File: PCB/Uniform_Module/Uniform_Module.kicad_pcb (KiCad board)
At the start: 2 copper layers, 33 x 16 mm, 17 parts, among them J1 PCIE_x1_Conn_01x36_Male, SW1 Button_SMD_PTS_647_SN50_SMTR2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, SW2 Button_SMD_PTS_647_SN50_SMTR2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, U1 STM32L072KZT6

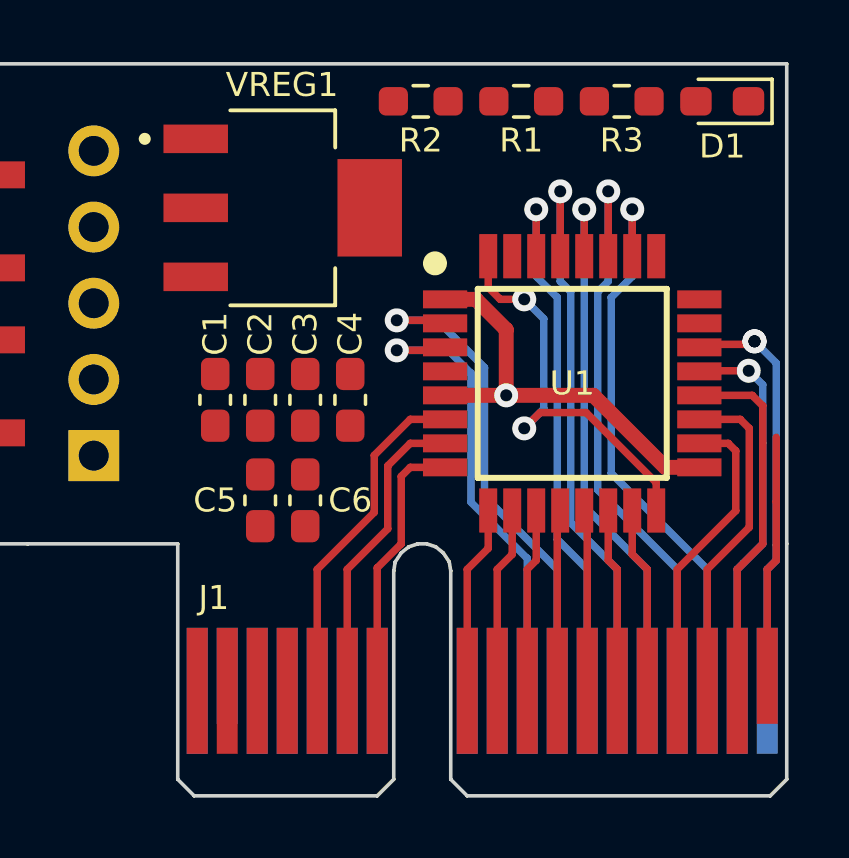
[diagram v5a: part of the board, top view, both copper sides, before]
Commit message: uniform module routing half done
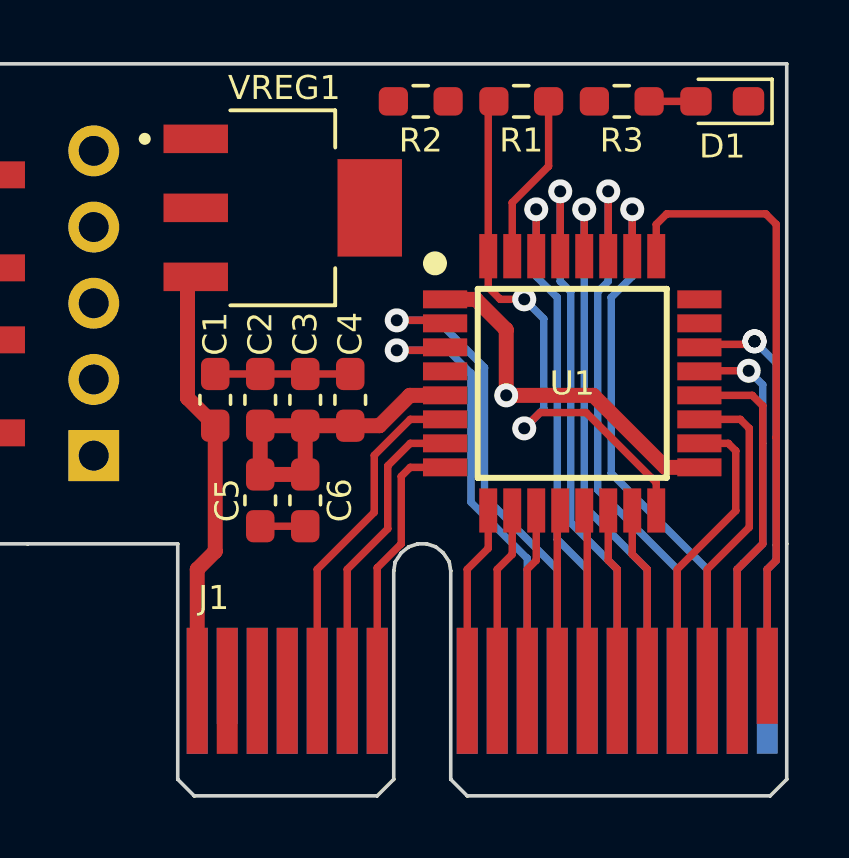
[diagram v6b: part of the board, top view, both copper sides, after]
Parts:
- turned C2 to 90 degrees
- turned C3 to 90 degrees
- turned C4 to 90 degrees
- turned C5 to -90 degrees
- turned C6 to -90 degrees
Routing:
- net +5V: track 0.00 -> 14.6 mm
- net PA15: track 8.07 -> 20.5 mm
- net GND: track 13.8 -> 25.1 mm
- net +3V3: track 14.1 -> 23.5 mm
- net BOOT: track 0.00 -> 5.66 mm
- net Net-(D1-Pad2): track 0.00 -> 1.56 mm

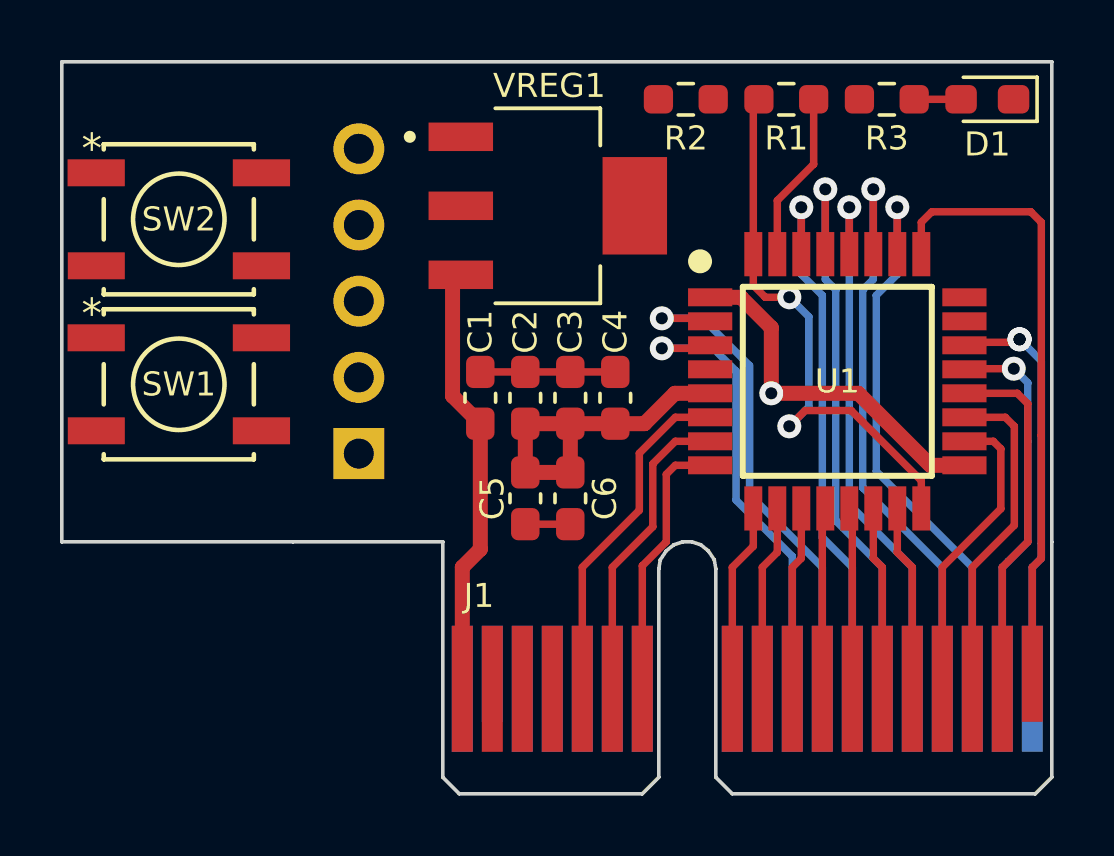
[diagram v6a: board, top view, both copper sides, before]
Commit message: Uniform module traces first pass complete
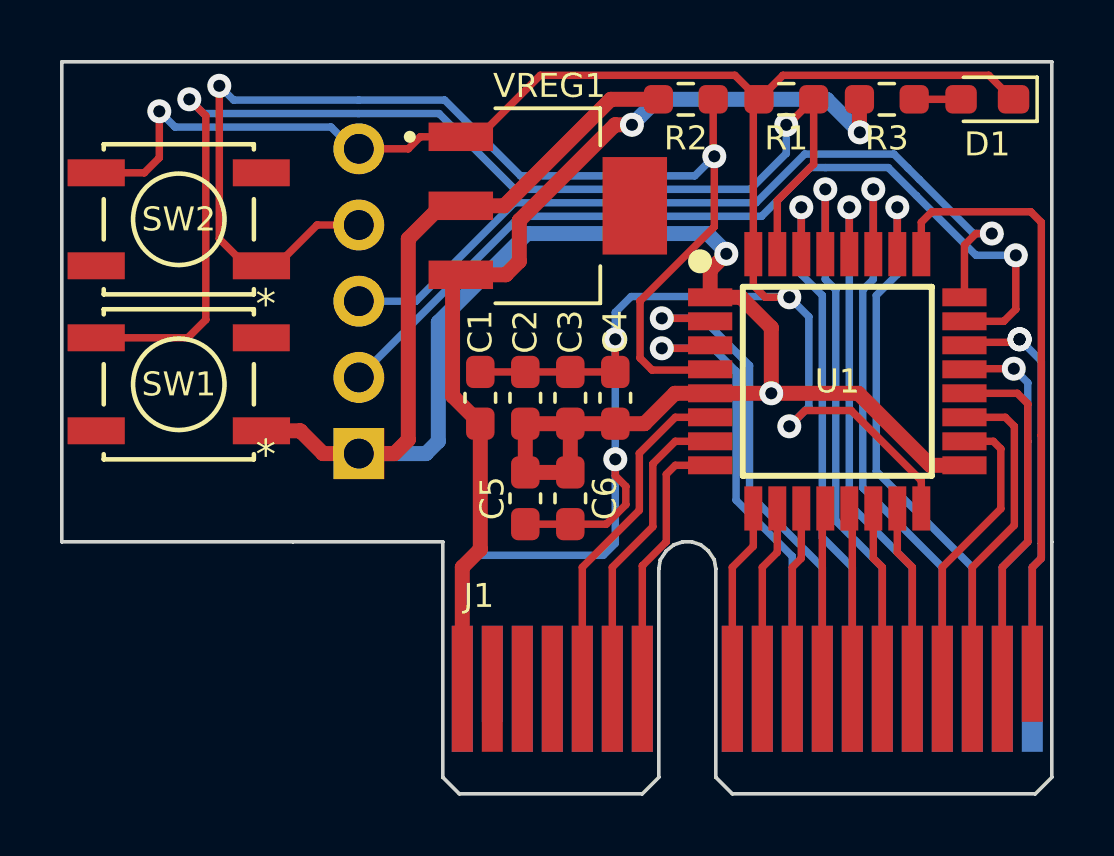
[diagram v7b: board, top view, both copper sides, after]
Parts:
- turned SW1 to 180 degrees
- turned SW2 to 180 degrees
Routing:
- net GND: track 25.1 -> 88.0 mm, vias 2 -> 5
- net +3V3: track 23.5 -> 67.5 mm, vias 1 -> 2
- net RESET: track 0.00 -> 40.9 mm, vias 0 -> 2
- net BOOT: track 5.66 -> 41.0 mm, vias 0 -> 2
- net SWDIO: track 0.00 -> 29.7 mm, vias 0 -> 1
- net SWCLK: track 0.00 -> 27.0 mm, vias 0 -> 1
- net +5V: track 14.6 -> 32.7 mm, vias 0 -> 2

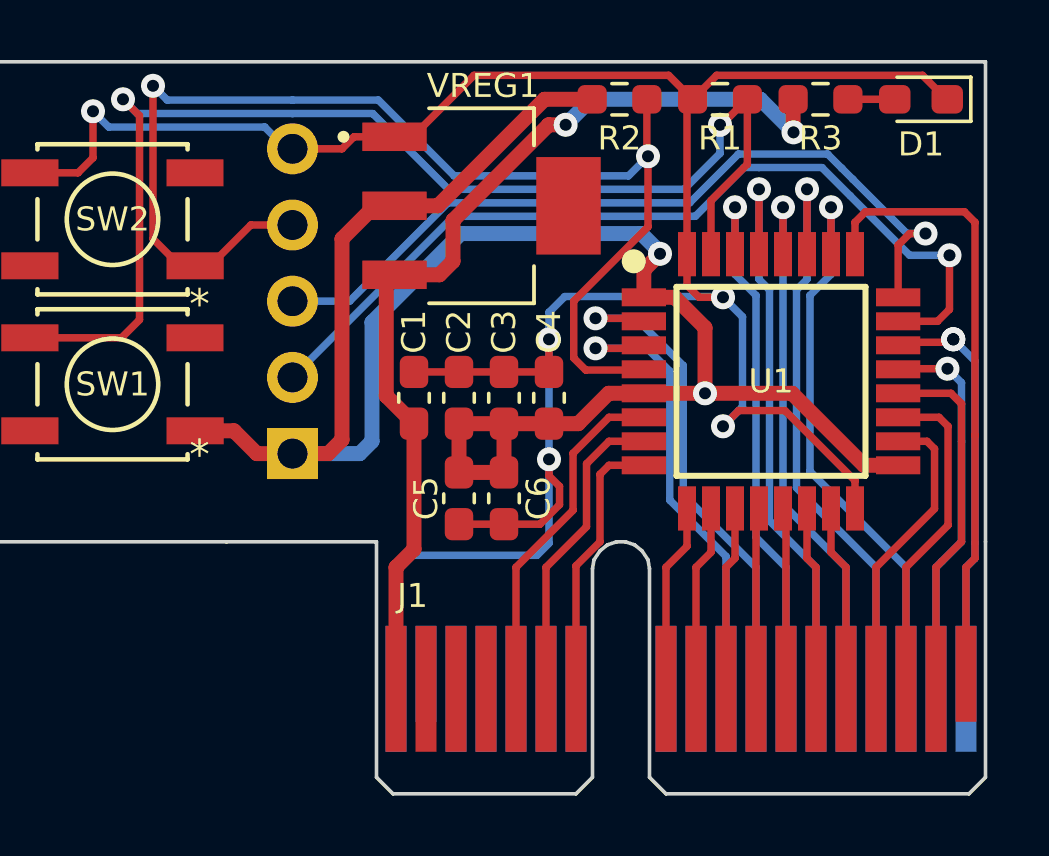
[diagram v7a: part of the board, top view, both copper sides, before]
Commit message: Uniform Module passing DRC
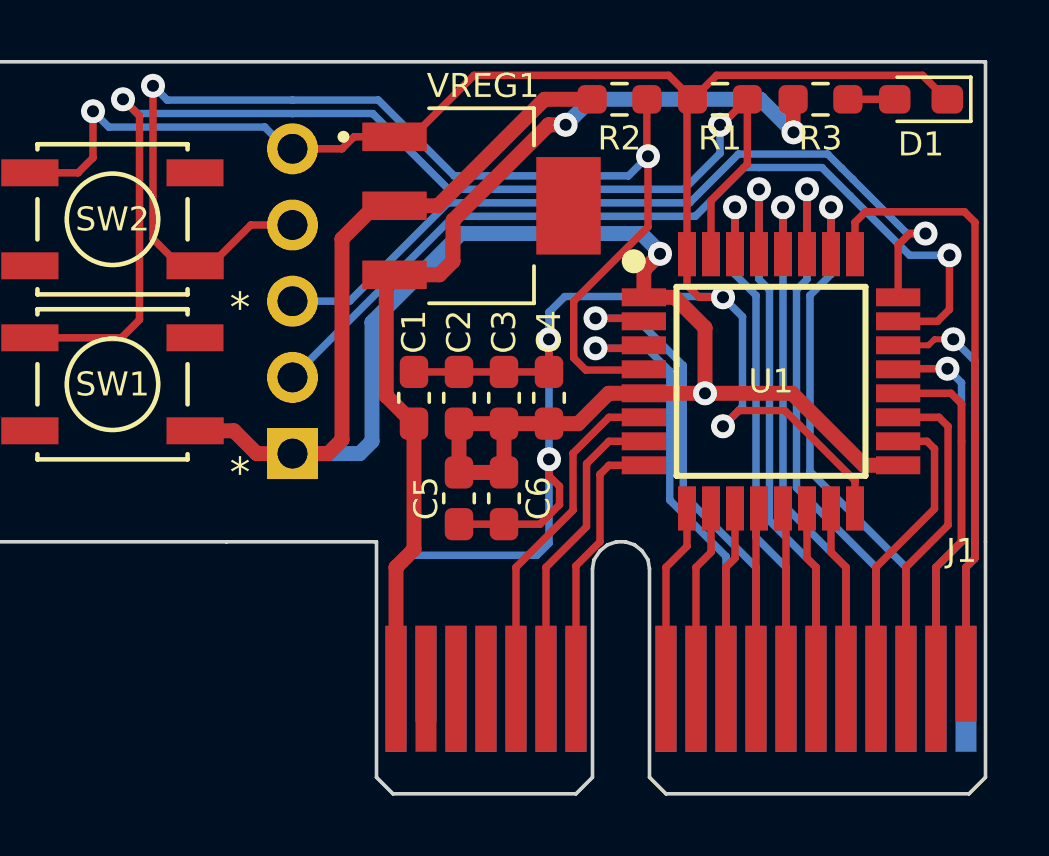
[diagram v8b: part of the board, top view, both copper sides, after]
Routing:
- net D_P: vias 2 -> 1
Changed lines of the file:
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@@
     (property "Sheetname" "")
     (attr smd)
-    (fp_text reference "J1" (at -8.45 -3.1 unlocked) (layer "F.SilkS")
+    (fp_text reference "J1" (at 9.85 -4.6 unlocked) (layer "F.SilkS")
       (effects (font (size 0.8 0.8) (thickness 0.15)))
     )
@@
       (effects (font (size 1 1) (thickness 0.15)))
     )
-    (fp_text user "*" (at -2.9 -2.35 180 unlocked) (layer "F.SilkS")
+    (fp_text user "*" (at -4.25 -2.95 unlocked) (layer "F.SilkS")
       (effects (font (size 1 1) (thickness 0.15)))
     )
@@
       (effects (font (size 1 1) (thickness 0.15)))
     )
-    (fp_text user "*" (at -2.9 -2.35) (layer "F.SilkS")
+    (fp_text user "*" (at -4.25 -2.95) (layer "F.SilkS")
       (effects (font (size 1 1) (thickness 0.15)))
     )
@@
   (segment (start 214.865 145.3975) (end 216.365 145.3975) (width 0.25) (layer "F.Cu") (net 1))
   (segment (start 223.45202 135.51048) (end 222.6525 136.31) (width 0.25) (layer "F.Cu") (net 1))
-  (segment (start 213.365 145.3975) (end 214.865 145.3975) (width 0.25) (layer "F.Cu") (net 1))
+  (segment (start 214.865 145.3975) (end 213.365 145.3975) (width 0.25) (layer "F.Cu") (net 1))
   (segment (start 222.465 136.4975) (end 222.6525 136.31) (width 0.25) (layer "F.Cu") (net 1))
   (segment (start 222.465 142.51) (end 222.465 141.472) (width 0.25) (layer "F.Cu") (net 1))
@@
   (segment (start 212.715 137.56) (end 213.315 137.56) (width 0.25) (layer "F.Cu") (net 1))
   (segment (start 225.728504 146.68452) (end 224.19048 146.68452) (width 0.25) (layer "F.Cu") (net 1))
-  (segment (start 213.365 145.3975) (end 213.365 145.51) (width 0.25) (layer "F.Cu") (net 1))
   (via (at 217.865 148.31) (size 0.8) (drill 0.4) (layers "F.Cu" "B.Cu") (net 1))
   (via (at 217.865 144.31) (size 0.8) (drill 0.4) (layers "F.Cu" "B.Cu") (net 1))
@@
   (segment (start 217.865 144.31) (end 217.865 143.41) (width 0.25) (layer "B.Cu") (net 1))
   (segment (start 208.390009 137.235009) (end 209.115 137.96) (width 0.25) (layer "B.Cu") (net 1))
-  (segment (start 212.765 155.96) (end 212.765 151.91) (width 0.25) (layer "B.Cu") (net 1))
   (segment (start 223.665 147.21) (end 224.31644 146.55856) (width 0.25) (layer "B.Cu") (net 1))
   (segment (start 203.190009 137.235009) (end 208.390009 137.235009) (width 0.25) (layer "B.Cu") (net 1))
   (segment (start 224.31644 146.55856) (end 224.31644 143.560064) (width 0.25) (layer "B.Cu") (net 1))
   (segment (start 217.865 151.11) (end 217.865 148.31) (width 0.25) (layer "B.Cu") (net 1))
+  (segment (start 212.765 155.96) (end 212.765 151.91) (width 0.25) (layer "B.Cu") (net 1))
   (segment (start 217.465 151.51) (end 217.865 151.11) (width 0.25) (layer "B.Cu") (net 1))
   (segment (start 224.31644 143.560064) (end 223.665688 142.909312) (width 0.25) (layer "B.Cu") (net 1))
@@
   (segment (start 212.44048 146.19798) (end 212.44048 142.43452) (width 0.5) (layer "F.Cu") (net 2))
   (segment (start 218.419988 137.1595) (end 217.85477 137.1595) (width 0.5) (layer "F.Cu") (net 2))
-  (segment (start 212.765 155.96) (end 212.765 151.91) (width 0.5) (layer "F.Cu") (net 2))
-  (segment (start 226.0025 136.31) (end 225.965 136.31) (width 0.5) (layer "F.Cu") (net 2))
+  (segment (start 212.765 151.91) (end 212.765 155.96) (width 0.5) (layer "F.Cu") (net 2))
   (segment (start 214.215 142.16) (end 212.715 142.16) (width 0.5) (layer "F.Cu") (net 2))
   (segment (start 214.665 141.71) (end 214.215 142.16) (width 0.5) (layer "F.Cu") (net 2))
@@
   (segment (start 224.91402 136.310489) (end 219.268999 136.310489) (width 0.5) (layer "B.Cu") (net 2))
   (segment (start 226.015 137.411469) (end 224.91402 136.310489) (width 0.5) (layer "B.Cu") (net 2))
-  (segment (start 214.865 148.7475) (end 214.865 147.1225) (width 0.5) (layer "F.Cu") (net 3))
   (segment (start 214.865 148.7475) (end 216.365 148.7475) (width 0.5) (layer "F.Cu") (net 3))
   (segment (start 219.852506 146.11) (end 221.027 146.11) (width 0.5) (layer "F.Cu") (net 3))
   (segment (start 221.027 142.91) (end 221.027 141.998498) (width 0.5) (layer "F.Cu") (net 3))
   (segment (start 209.315 148.12) (end 210.505 148.12) (width 0.5) (layer "F.Cu") (net 3))
-  (segment (start 214.865 147.1225) (end 216.365 147.1225) (width 0.5) (layer "F.Cu") (net 3))
+  (segment (start 223.065 146.11) (end 223.065 143.922494) (width 0.5) (layer "F.Cu") (net 3))
   (segment (start 221.027 141.998498) (end 221.565498 141.46) (width 0.5) (layer "F.Cu") (net 3))
   (segment (start 221.027 142.91) (end 222.052506 142.91) (width 0.5) (layer "F.Cu") (net 3))
   (segment (start 210.505 148.12) (end 210.965 147.66) (width 0.5) (layer "F.Cu") (net 3))
   (segment (start 210.965 147.66) (end 210.965 140.96) (width 0.5) (layer "F.Cu") (net 3))
-  (segment (start 223.065 143.922494) (end 223.065 146.11) (width 0.5) (layer "F.Cu") (net 3))
   (segment (start 216.365 148.7475) (end 216.365 147.1225) (width 0.5) (layer "F.Cu") (net 3))
   (segment (start 214.165 139.86) (end 217.715 136.31) (width 0.5) (layer "F.Cu") (net 3))
+  (segment (start 216.365 147.1225) (end 214.865 147.1225) (width 0.5) (layer "F.Cu") (net 3))
   (segment (start 217.865 147.1225) (end 218.840006 147.1225) (width 0.5) (layer "F.Cu") (net 3))
   (segment (start 228.366478 148.51) (end 225.966478 146.11) (width 0.5) (layer "F.Cu") (net 3))
-  (segment (start 225.966478 146.11) (end 223.065 146.11) (width 0.5) (layer "F.Cu") (net 3))
   (segment (start 218.840006 147.1225) (end 219.852506 146.11) (width 0.5) (layer "F.Cu") (net 3))
-  (segment (start 214.865 147.01) (end 214.865 147.1225) (width 0.25) (layer "F.Cu") (net 3))
-  (segment (start 223.065 146.11) (end 221.027 146.11) (width 0.5) (layer "F.Cu") (net 3))
   (segment (start 207.365 147.36) (end 208.125 148.12) (width 0.5) (layer "F.Cu") (net 3))
-  (segment (start 206.0692 147.36) (end 207.365 147.36) (width 0.5) (layer "F.Cu") (net 3))
   (segment (start 212.715 139.86) (end 214.165 139.86) (width 0.5) (layer "F.Cu") (net 3))
   (segment (start 222.052506 142.91) (end 223.065 143.922494) (width 0.5) (layer "F.Cu") (net 3))
@@
   (segment (start 208.125 148.12) (end 209.315 148.12) (width 0.5) (layer "F.Cu") (net 3))
   (segment (start 217.715 136.31) (end 219.3025 136.31) (width 0.5) (layer "F.Cu") (net 3))
+  (segment (start 207.365 147.36) (end 206.0692 147.36) (width 0.5) (layer "F.Cu") (net 3))
+  (segment (start 221.027 146.11) (end 223.065 146.11) (width 0.5) (layer "F.Cu") (net 3))
   (segment (start 210.965 140.96) (end 212.065 139.86) (width 0.5) (layer "F.Cu") (net 3))
   (segment (start 229.503 148.51) (end 228.366478 148.51) (width 0.5) (layer "F.Cu") (net 3))
+  (segment (start 223.065 146.11) (end 225.966478 146.11) (width 0.5) (layer "F.Cu") (net 3))
   (segment (start 212.065 139.86) (end 212.715 139.86) (width 0.5) (layer "F.Cu") (net 3))
+  (segment (start 214.865 148.7475) (end 214.865 147.1225) (width 0.5) (layer "F.Cu") (net 3))
   (via (at 223.065 146.11) (size 0.8) (drill 0.4) (layers "F.Cu" "B.Cu") (net 3))
   (via (at 221.565498 141.46) (size 0.8) (drill 0.4) (layers "F.Cu" "B.Cu") (net 3))
@@
   (segment (start 204.140489 136.785489) (end 203.665 136.31) (width 0.25) (layer "B.Cu") (net 44))
   (segment (start 211.990489 136.785489) (end 209.315 136.785489) (width 0.25) (layer "B.Cu") (net 44))
-  (segment (start 229.603 144.41) (end 229.503 144.51) (width 0.25) (layer "F.Cu") (net 45))
-  (segment (start 231.3405 144.31) (end 231.165 144.31) (width 0.25) (layer "F.Cu") (net 45))
-  (segment (start 231.165 144.31) (end 231.065 144.41) (width 0.25) (layer "F.Cu") (net 45))
-  (segment (start 231.065 144.41) (end 229.603 144.41) (width 0.25) (layer "F.Cu") (net 45))
-  (via (at 231.3405 144.31) (size 0.8) (drill 0.4) (layers "F.Cu" "B.Cu") (net 45))
-  (via (at 231.3405 144.31) (size 0.8) (drill 0.4) (layers "F.Cu" "B.Cu") (net 45))
+  (segment (start 230.715 144.31) (end 231.340511 144.31) (width 0.2) (layer "F.Cu") (net 45))
+  (segment (start 230.515 144.51) (end 230.715 144.31) (width 0.2) (layer "F.Cu") (net 45))
+  (segment (start 229.503 144.51) (end 230.515 144.51) (width 0.2) (layer "F.Cu") (net 45))
+  (via (at 231.340511 144.31) (size 0.8) (drill 0.4) (layers "F.Cu" "B.Cu") (net 45))
   (segment (start 232.065 145.0345) (end 231.3405 144.31) (width 0.25) (layer "B.Cu") (net 45))
   (segment (start 232.065 151.61) (end 232.065 151.11) (width 0.25) (layer "B.Cu") (net 45))
   (segment (start 232.065 151.11) (end 232.065 145.0345) (width 0.25) (layer "B.Cu") (net 45))
+  (segment (start 231.3405 144.31) (end 231.340511 144.31) (width 0.2) (layer "B.Cu") (net 45))
   (segment (start 231.765 151.91) (end 232.065 151.61) (width 0.25) (layer "B.Cu") (net 45))
   (segment (start 231.765 155.96) (end 231.765 151.91) (width 0.25) (layer "B.Cu") (net 45))
